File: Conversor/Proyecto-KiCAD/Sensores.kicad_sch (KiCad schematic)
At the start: 27 parts

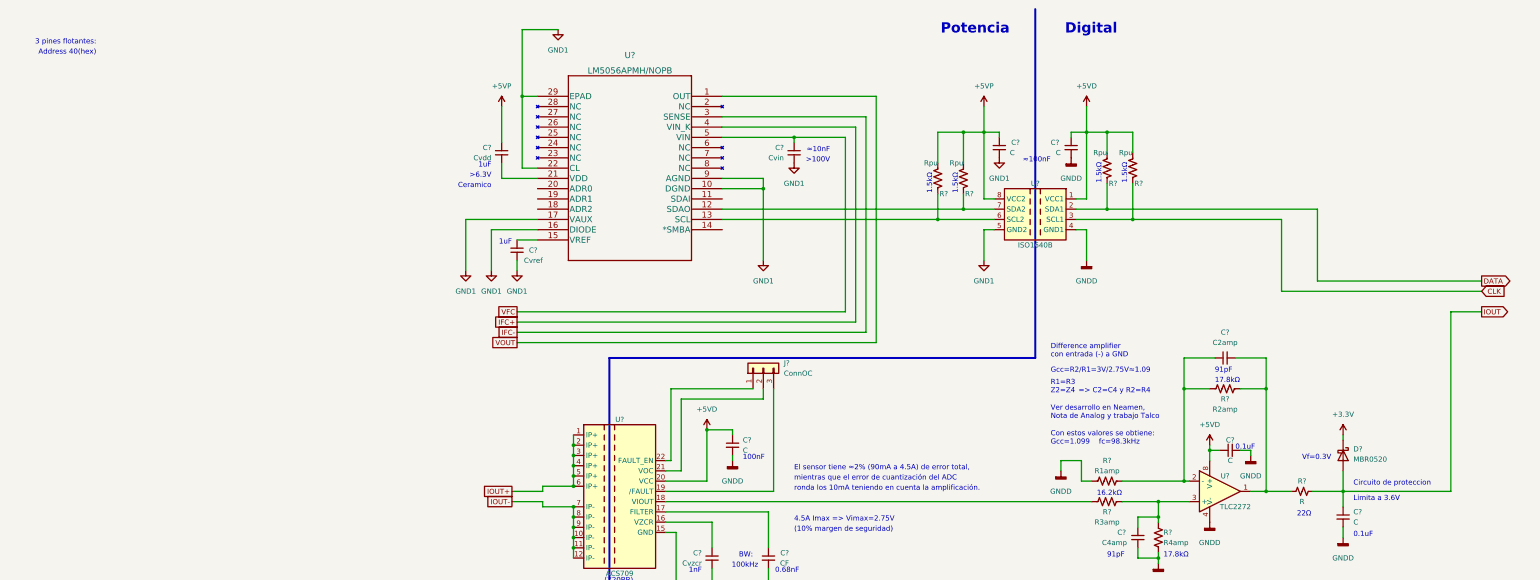
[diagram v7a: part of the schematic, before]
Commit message: Reemplazar ISO1641 por aislador SI8642 (en stock)
- Agregar su datasheet y incluirlo en la lista de componentes
- Conectar tambien la linea de recepcion de datos del LM5056A
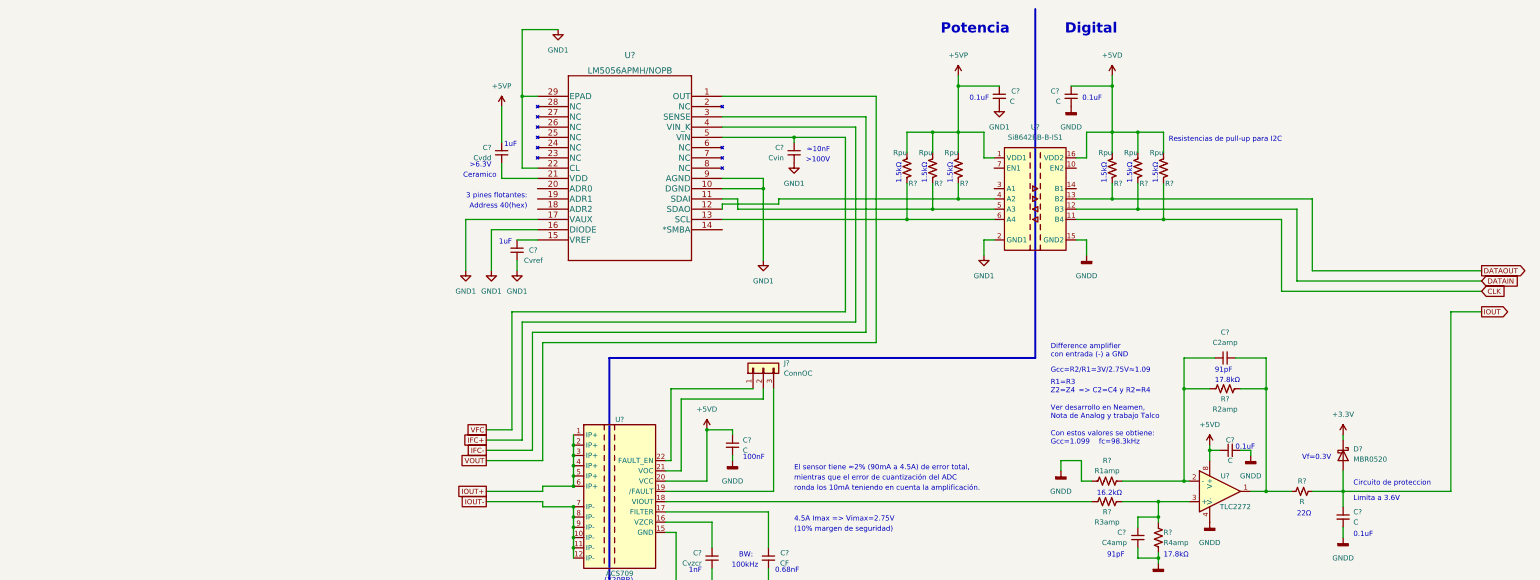
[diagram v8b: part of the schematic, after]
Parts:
- removed U?: ISO1640B, Package_SO:SOIC-8_3.9x4.9mm_P1.27mm, symbol Componentes proyecto:ISO1640B
- added R? (x2): Rpu, symbol Device:R_US
- added U?: Si8642BB-B-IS1, Package_SO:SOIC-16_3.9x9.9mm_P1.27mm, symbol Isolator:Si8642BB-B-IS1
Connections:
- net +5VD: now also R?.1, U?.16 (VDD2)
- net +5VP: now also R?.1, U?.1 (VDD1)
- net CLK: now also U?.11 (B4)
- net GND1: now also U?.2 (GND1), U?.8 (GND1)
- net GNDD: now also U?.15 (GND2), U?.9 (GND2)
- net at R?.2, U?.13 (SCL): now also U?.6 (A4)
- net at R?.2, U?.12 (SDAO): now also U?.4 (A2)
- net at U?.11 (SDAI): now also R?.2, U?.5 (A3)
- net DATA renamed DATAIN
- net DATAIN: now also U?.12 (B3)
- new net DATAOUT: R?.2, U?.13 (B2)
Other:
- note added: "Resistencias de pull-up para I2C"
- note removed: "≈100nF"
- moved on the sheet: C?, R?
